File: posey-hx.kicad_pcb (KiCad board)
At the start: 4 copper layers, 37 x 35.6 mm, 33 parts, among them J1 TC2050-IDC-NL, U1 NORA-B106-00B, U2 W25N01GVZEIG_TR, Y1 XTAL, Y2 XTAL

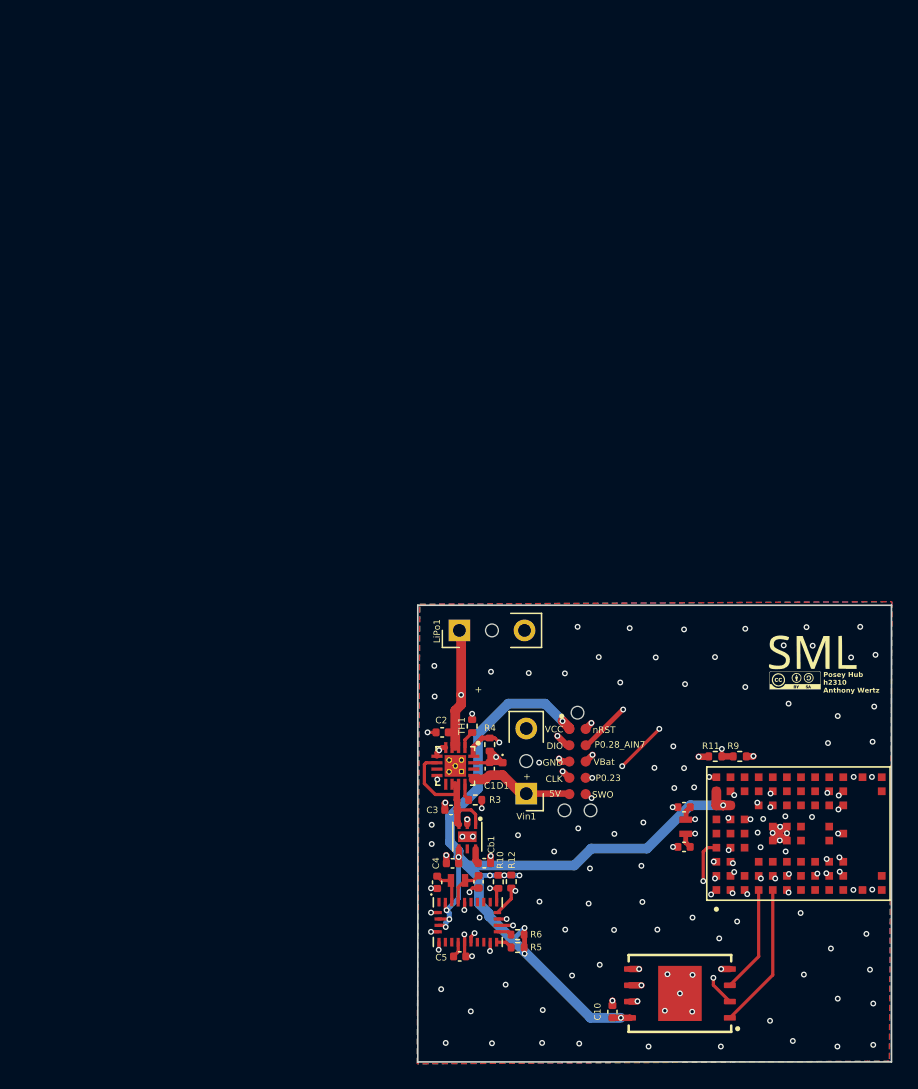
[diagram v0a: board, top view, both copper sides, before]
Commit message: Updated readme, license, and version.
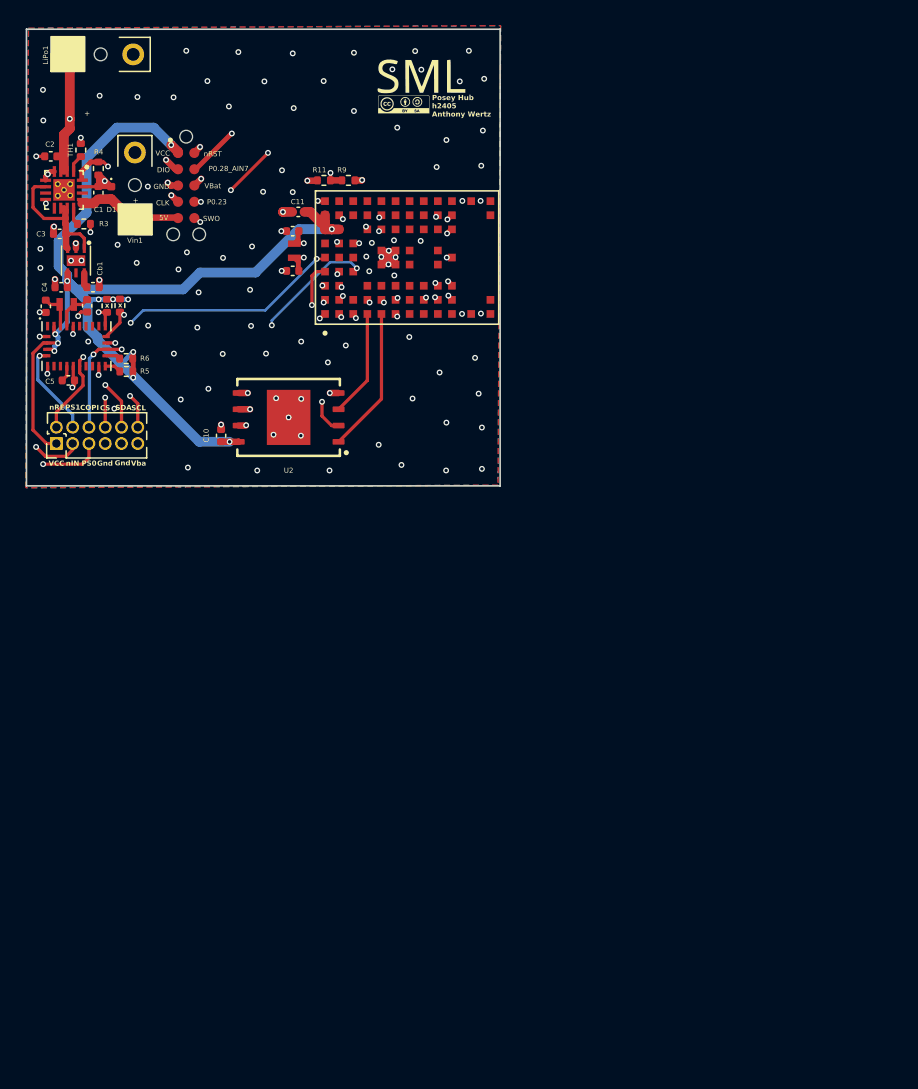
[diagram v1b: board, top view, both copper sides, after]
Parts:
- added C11: 0.1µ, Capacitor_SMD:C_0402_1005Metric, F.Cu at (145.6, 91.8)
- added J2: Conn_02x06_Odd_Even, Connector_PinHeader_1.27mm:PinHeader_2x06_P1.27mm_Vertical, F.Cu at (126.7, 109.9)
- IMU1: value BNO080 -> BNO085/6
- moved C3 54.3 mm to (126.9, 93.6)
- moved Cb1 54.3 mm to (129.5, 97.7)
- moved J1 54.3 mm to (136.2, 87.2)
- moved C1 54.3 mm to (130.0, 90.3)
- moved C2 54.3 mm to (126.2, 87.5)
- moved C4 54.3 mm to (127.1, 97.7)
- moved C7 54.3 mm to (129.1, 99.2)
- moved CHRG1 54.3 mm to (127.3, 90.1)
- moved LiPo1 54.3 mm to (127.6, 79.5)
- moved R3 54.3 mm to (128.8, 92.8)
- moved R5 54.3 mm to (132.1, 104.3)
- moved REG1 54.3 mm to (128.2, 95.6)
- moved U1 54.3 mm to (153.1, 95.4)
- moved U2 54.3 mm to (144.8, 107.9)
- moved Vin1 54.3 mm to (132.8, 92.3)
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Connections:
- IMU1 pad 5: GND -> IMU_PS1
- IMU1 pad 6: GND -> IMU_PS0
- U1 pad A5: unconnected-(U1-P0.20-PadA5) -> IMU_PS1
- U1 pad C4: unconnected-(U1-P1.01-PadC4) -> IMU_PS0
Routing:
- net IMU_PS0: track 0.00 -> 41.2 mm, vias 0 -> 4
- net IMU_PS1: track 0.00 -> 33.1 mm, vias 0 -> 3
- net VBAT: track 31.1 -> 54.3 mm
- net IMU_nINT: track 22.6 -> 34.3 mm, vias 2 -> 3
- net VCC: track 82.0 -> 93.6 mm
- net SCL/SPI_SCK: track 19.2 -> 29.3 mm, vias 2 -> 3
- net SDA/SPI_CIPO: track 21.6 -> 31.4 mm, vias 2 -> 3
- net SPI_COPI: track 18.5 -> 25.5 mm, vias 2 -> 3
- net SPI_CS_IMU: track 20.7 -> 27.6 mm, vias 2 -> 3
- net IMU_nRESET: track 22.6 -> 28.3 mm
- net SWO: track 16.4 -> 14.9 mm
- net GND: track 32.4 -> 31.5 mm, vias 128 -> 119
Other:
- board text added: "COPI"
- board text added: "CS"
- board text added: "Gnd"
- board text added: "PS0"
- board text added: "PS1"
- board text added: "Posey Hub h2405 Anthony Wertz"
- board text added: "SCL"
- board text added: "SDA"
- board text added: "Vba"
- board text added: "nIN"
- board text added: "nRE"
- board text added: "x"
- board text removed: "Posey Hub h2310 Anthony Wertz"
